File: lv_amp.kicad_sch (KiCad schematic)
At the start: 80 parts, among them J1 AudioJack2, J2 Jack-DC, J3 AudioJack2, Q1 Q_NMOS_DGS, U1 ECC83, U2 TL072, U3 ECC83, U4 ECC83, U5 MAX1771xSA

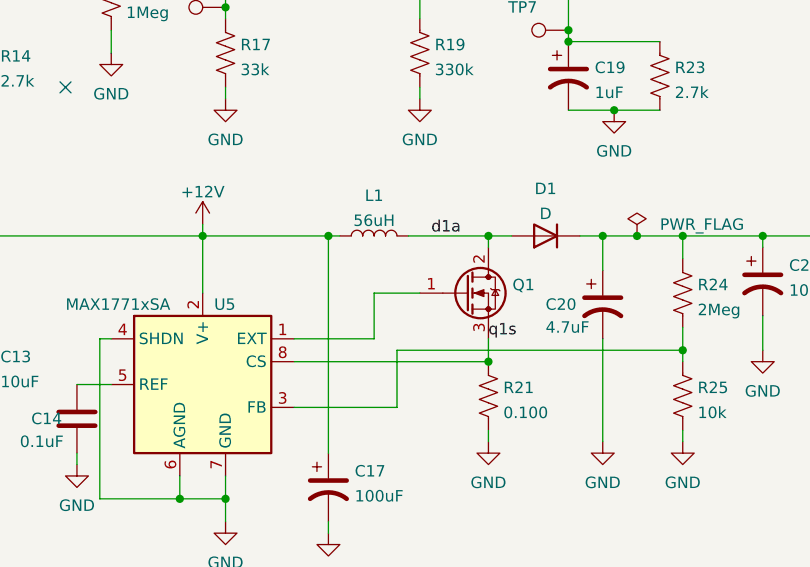
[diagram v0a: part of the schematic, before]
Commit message: power supply layout
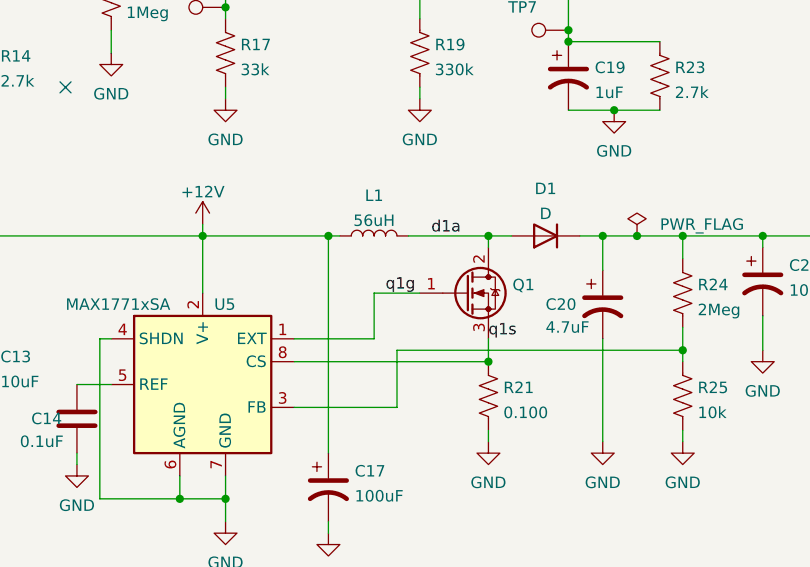
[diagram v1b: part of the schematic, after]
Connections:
- net q1g: now reaches Q1.1 (G), U5.1 (EXT)
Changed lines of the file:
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@@
+    (effects (font (size 1.27 1.27)) (justify left bottom))
+  )
+  (label "q1g" (at 170.18 125.73 0)
     (effects (font (size 1.27 1.27)) (justify left bottom))
   )

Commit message: tighter layout
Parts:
- removed TP1, TP5, TP6, TP7, TP8: TestPoint, TestPoint:TestPoint_THTPad_2.0x2.0mm_Drill1.0mm, symbol Connector:TestPoint
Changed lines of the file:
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@@
   (junction (at 85.09 157.48) (diameter 0) (color 0 0 0 0)
   )
-  (junction (at 152.4 93.98) (diameter 0) (color 0 0 0 0)
-  )
   (junction (at 48.26 143.51) (diameter 0) (color 0 0 0 0)
   )
@@
   (junction (at 193.04 69.85) (diameter 0) (color 0 0 0 0)
   )
-  (junction (at 190.5 96.52) (diameter 0) (color 0 0 0 0)
-  )
   (junction (at 194.31 119.38) (diameter 0) (color 0 0 0 0)
   )
@@
   (junction (at 29.21 152.4) (diameter 0) (color 0 0 0 0)
   )
-  (junction (at 240.03 93.98) (diameter 0) (color 0 0 0 0)
-  )
   (junction (at 267.97 76.2) (diameter 0) (color 0 0 0 0)
   )
@@
   (junction (at 64.77 160.02) (diameter 0) (color 0 0 0 0)
   )
-  (junction (at 115.57 95.25) (diameter 0) (color 0 0 0 0)
-  )
   (junction (at 59.69 72.39) (diameter 0) (color 0 0 0 0)
   )
@@
   (junction (at 154.94 189.23) (diameter 0) (color 0 0 0 0)
   )
-  (junction (at 57.15 96.52) (diameter 0) (color 0 0 0 0)
-  )
   (junction (at 73.66 72.39) (diameter 0) (color 0 0 0 0)
   )
@@
     (stroke (width 0) (type default) (color 0 0 0 0))
   )
-  (wire (pts (xy 115.57 95.25) (xy 115.57 96.52))
+  (wire (pts (xy 115.57 92.71) (xy 115.57 96.52))
     (stroke (width 0) (type default) (color 0 0 0 0))
   )
-  (wire (pts (xy 152.4 93.98) (xy 152.4 95.25))
+  (wire (pts (xy 152.4 92.71) (xy 152.4 95.25))
     (stroke (width 0) (type default) (color 0 0 0 0))
   )
@@
     (stroke (width 0) (type default) (color 0 0 0 0))
   )
-  (wire (pts (xy 190.5 92.71) (xy 190.5 96.52))
+  (wire (pts (xy 190.5 92.71) (xy 190.5 97.79))
     (stroke (width 0) (type default) (color 0 0 0 0))
   )
@@
     (stroke (width 0) (type default) (color 0 0 0 0))
   )
-  (wire (pts (xy 57.15 96.52) (xy 57.15 97.79))
+  (wire (pts (xy 57.15 93.98) (xy 57.15 97.79))
     (stroke (width 0) (type default) (color 0 0 0 0))
   )
@@
     (stroke (width 0) (type default) (color 0 0 0 0))
   )
-  (wire (pts (xy 57.15 93.98) (xy 57.15 96.52))
-    (stroke (width 0) (type default) (color 0 0 0 0))
-  )
   (wire (pts (xy 82.55 72.39) (xy 85.09 72.39))
     (stroke (width 0) (type default) (color 0 0 0 0))
@@
     (stroke (width 0) (type default) (color 0 0 0 0))
   )
-  (wire (pts (xy 115.57 92.71) (xy 115.57 95.25))
-    (stroke (width 0) (type default) (color 0 0 0 0))
-  )
   (wire (pts (xy 73.66 72.39) (xy 73.66 63.5))
     (stroke (width 0) (type default) (color 0 0 0 0))
@@
     (stroke (width 0) (type default) (color 0 0 0 0))
   )
-  (wire (pts (xy 152.4 92.71) (xy 152.4 93.98))
-    (stroke (width 0) (type default) (color 0 0 0 0))
-  )
   (wire (pts (xy 35.56 96.52) (xy 35.56 100.33))
     (stroke (width 0) (type default) (color 0 0 0 0))
@@
     (stroke (width 0) (type default) (color 0 0 0 0))
   )
-  (wire (pts (xy 240.03 90.17) (xy 240.03 93.98))
+  (wire (pts (xy 240.03 90.17) (xy 240.03 95.25))
     (stroke (width 0) (type default) (color 0 0 0 0))
   )
@@
     (stroke (width 0) (type default) (color 0 0 0 0))
   )
-  (wire (pts (xy 240.03 93.98) (xy 240.03 95.25))
-    (stroke (width 0) (type default) (color 0 0 0 0))
-  )
   (wire (pts (xy 118.11 40.64) (xy 118.11 44.45))
     (stroke (width 0) (type default) (color 0 0 0 0))
   )
-  (wire (pts (xy 190.5 96.52) (xy 190.5 97.79))
-    (stroke (width 0) (type default) (color 0 0 0 0))
-  )
   (wire (pts (xy 57.15 97.79) (xy 67.31 97.79))
     (stroke (width 0) (type default) (color 0 0 0 0))
@@
     (pin "1")
   )
-  (symbol (lib_id "Connector:TestPoint") (at 190.5 96.52 90) (unit 1)
-    (in_bom yes) (on_board yes)
-    (property "Reference" "TP7" (id 0) (at 185.42 93.98 90))
-    (property "Value" "TestPoint" (id 1) (at 187.198 94.6936 90)
-      (effects (font (size 1.27 1.27)) hide)
-    )
-    (property "Footprint" "TestPoint:TestPoint_THTPad_2.0x2.0mm_Drill1.0mm" (id 2) (at 190.5 91.44 0)
-      (effects (font (size 1.27 1.27)) hide)
-    )
-    (property "Datasheet" "~" (id 3) (at 190.5 91.44 0)
-      (effects (font (size 1.27 1.27)) hide)
-    )
-    (pin "1")
-  )
   (symbol (lib_id "power:+12V") (at 111.76 43.18 180) (unit 1)
     (in_bom yes) (on_board yes) (fields_autoplaced)
@@
     (pin "1")
   )
-  (symbol (lib_id "Connector:TestPoint") (at 152.4 93.98 90) (unit 1)
-    (in_bom yes) (on_board yes)
-    (property "Reference" "TP6" (id 0) (at 148.59 91.44 90))
-    (property "Value" "TestPoint" (id 1) (at 149.098 92.1536 90)
-      (effects (font (size 1.27 1.27)) hide)
-    )
-    (property "Footprint" "TestPoint:TestPoint_THTPad_2.0x2.0mm_Drill1.0mm" (id 2) (at 152.4 88.9 0)
-      (effects (font (size 1.27 1.27)) hide)
-    )
-    (property "Datasheet" "~" (id 3) (at 152.4 88.9 0)
-      (effects (font (size 1.27 1.27)) hide)
-    )
-    (pin "1")
-  )
   (symbol (lib_id "power:PWR_FLAG") (at 109.22 119.38 180) (unit 1)
     (in_bom yes) (on_board yes) (fields_autoplaced)
@@
     (pin "2")
   )
-  (symbol (lib_id "Connector:TestPoint") (at 240.03 93.98 90) (unit 1)
-    (in_bom yes) (on_board yes)
-    (property "Reference" "TP8" (id 0) (at 234.95 91.44 90))
-    (property "Value" "TestPoint" (id 1) (at 236.728 92.1536 90)
-      (effects (font (size 1.27 1.27)) hide)
-    )
-    (property "Footprint" "TestPoint:TestPoint_THTPad_2.0x2.0mm_Drill1.0mm" (id 2) (at 240.03 88.9 0)
-      (effects (font (size 1.27 1.27)) hide)
-    )
-    (property "Datasheet" "~" (id 3) (at 240.03 88.9 0)
-      (effects (font (size 1.27 1.27)) hide)
-    )
-    (pin "1")
-  )
   (symbol (lib_id "power:HT") (at 118.11 44.45 180) (unit 1)
     (in_bom yes) (on_board yes) (fields_autoplaced)
@@
     (pin "1")
   )
-  (symbol (lib_id "Connector:TestPoint") (at 57.15 96.52 90) (unit 1)
-    (in_bom yes) (on_board yes)
-    (property "Reference" "TP1" (id 0) (at 52.07 93.98 90))
-    (property "Value" "TestPoint" (id 1) (at 53.848 94.6936 90)
-      (effects (font (size 1.27 1.27)) hide)
-    )
-    (property "Footprint" "TestPoint:TestPoint_THTPad_2.0x2.0mm_Drill1.0mm" (id 2) (at 57.15 91.44 0)
-      (effects (font (size 1.27 1.27)) hide)
-    )
-    (property "Datasheet" "~" (id 3) (at 57.15 91.44 0)
-      (effects (font (size 1.27 1.27)) hide)
-    )
-    (pin "1")
-  )
   (symbol (lib_id "Device:C_Polarized_US") (at 124.46 134.62 0) (unit 1)
     (in_bom yes) (on_board yes) (fields_autoplaced)
@@
     (pin "1")
   )
-  (symbol (lib_id "Connector:TestPoint") (at 115.57 95.25 90) (unit 1)
-    (in_bom yes) (on_board yes)
-    (property "Reference" "TP5" (id 0) (at 110.49 92.71 90))
-    (property "Value" "TestPoint" (id 1) (at 112.268 93.4236 90)
-      (effects (font (size 1.27 1.27)) hide)
-    )
-    (property "Footprint" "TestPoint:TestPoint_THTPad_2.0x2.0mm_Drill1.0mm" (id 2) (at 115.57 90.17 0)
-      (effects (font (size 1.27 1.27)) hide)
-    )
-    (property "Datasheet" "~" (id 3) (at 115.57 90.17 0)
-      (effects (font (size 1.27 1.27)) hide)
-    )
-    (pin "1")
-  )
   (symbol (lib_id "Valve:ECC83") (at 73.66 29.21 0) (unit 3)
     (in_bom yes) (on_board yes) (fields_autoplaced)
@@
       (reference "RV4") (unit 1) (value "500k") (footprint "Potentiometer_THT:Potentiometer_Piher_T-16H_Single_Horizontal")
     )
-    (path "/72b96fdc-17eb-4ecb-ae5d-68b51cd75350"
-      (reference "TP1") (unit 1) (value "TestPoint") (footprint "TestPoint:TestPoint_THTPad_2.0x2.0mm_Drill1.0mm")
-    )
     (path "/6e1639bd-21ca-4f2f-b6f4-6dbea494eb53"
       (reference "TP2") (unit 1) (value "TestPoint") (footprint "TestPoint:TestPoint_THTPad_2.0x2.0mm_Drill1.0mm")
@@
       (reference "TP4") (unit 1) (value "TestPoint") (footprint "TestPoint:TestPoint_THTPad_2.0x2.0mm_Drill1.0mm")
     )
-    (path "/beffb8e8-cbb0-4bb3-bc79-ad300693e67c"
-      (reference "TP5") (unit 1) (value "TestPoint") (footprint "TestPoint:TestPoint_THTPad_2.0x2.0mm_Drill1.0mm")
-    )
-    (path "/1d857cb6-ac9c-45f8-a53f-50be7ba59418"
-      (reference "TP6") (unit 1) (value "TestPoint") (footprint "TestPoint:TestPoint_THTPad_2.0x2.0mm_Drill1.0mm")
-    )
-    (path "/0fc25247-064e-4a99-a2d0-b21a85dfd649"
-      (reference "TP7") (unit 1) (value "TestPoint") (footprint "TestPoint:TestPoint_THTPad_2.0x2.0mm_Drill1.0mm")
-    )
-    (path "/5d591f3c-2404-4803-a07e-13d37c52af18"
-      (reference "TP8") (unit 1) (value "TestPoint") (footprint "TestPoint:TestPoint_THTPad_2.0x2.0mm_Drill1.0mm")
-    )
     (path "/24fe7676-0c0a-4b5a-8a61-dd833b2a3e83"

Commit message: route/re-annotate
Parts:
- added H1, H2, H3, H4: MountingHole_Pad, MountingHole:MountingHole_3.2mm_M3, symbol Mechanical:MountingHole_Pad
- renumbered C22 to C1, C5 to C11, C7 to C12, C3 to C13, C2 to C14, C8 to C15, C23 to C16, C12 to C17, C9 to C18, C16 to C19, C1 to C2, C21 to C20, C18 to C21, C4 to C22, C6 to C23, C19 to C3, C13 to C4, C20 to C5, C11 to C6, C14 to C7, C17 to C8, C15 to C9, J2 to J1, J3 to J2, J1 to J3, R32 to R1, R21 to R10, R28 to R11, R27 to R12, R26 to R13, R15 to R14, R18 to R15, R12 to R17, R22 to R18, R7 to R19, R31 to R2, R14 to R20, R5 to R21, R4 to R22, R13 to R23, R8 to R24, R3 to R25, R2 to R26, R9 to R27, R17 to R28, R20 to R29, R30 to R3, R6 to R30, R19 to R31, R10 to R32, R11 to R33, R29 to R4, R25 to R5, R24 to R6, R1 to R7, R33 to R8, R23 to R9, RV4 to RV1, RV1 to RV3, RV3 to RV4, TP4 to TP1, TP9 to TP4, U5 to U1, U4 to U3, U3 to U4, U1 to U5
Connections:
- net GND: now also H1.1, H2.1, H3.1, H4.1

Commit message: tweaks
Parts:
- renumbered C23 to C21, C21 to C22, C22 to C23, R11 to R10, R10 to R11, R17 to R15, R18 to R16, R15 to R17, R16 to R18, R20 to R19, R19 to R20, R23 to R22, R24 to R23, R22 to R24, R27 to R26, R29 to R27, R26 to R29, R7 to R4, R8 to R5, R4 to R6, R5 to R7, R6 to R8

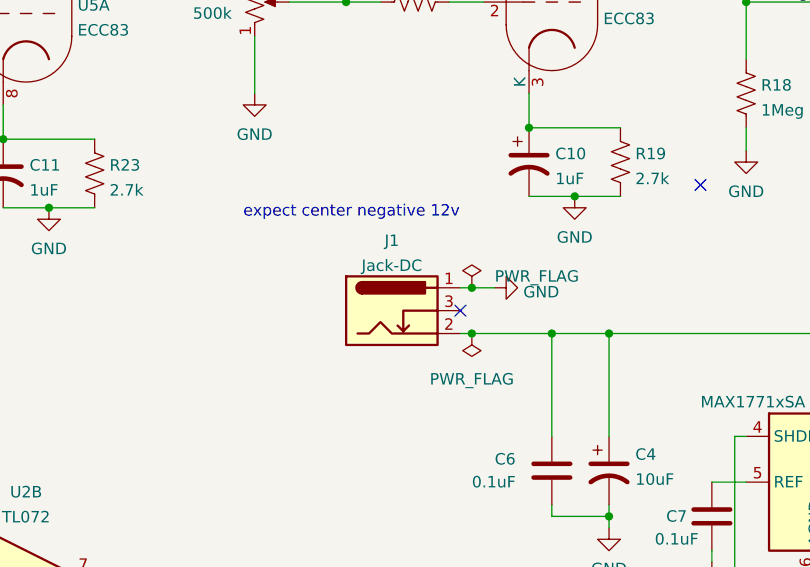
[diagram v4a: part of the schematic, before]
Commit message: alpha0 errata: DC jack
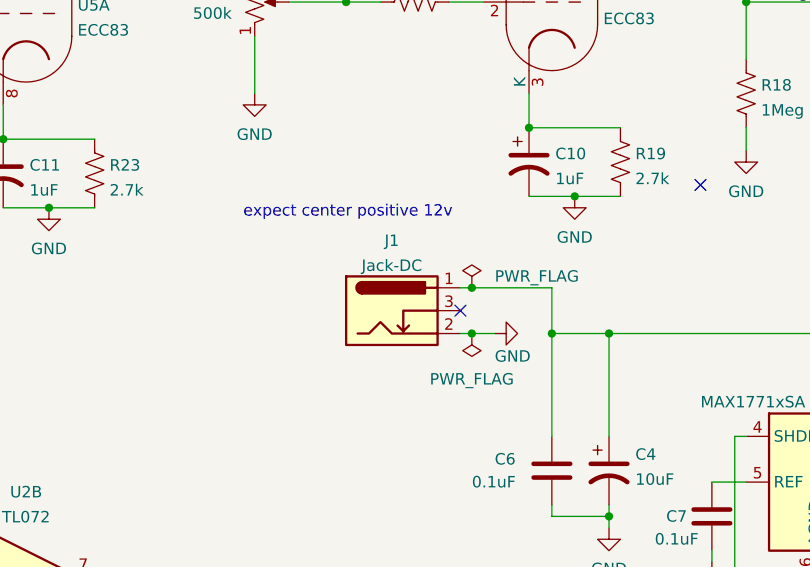
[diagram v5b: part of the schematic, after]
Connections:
- net +12V: now also J1.1; no longer J1.2
- net GND: now also J1.2; no longer J1.1
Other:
- note added: "expect center positive 12v"
- note removed: "expect center negative 12v"
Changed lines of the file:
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@@
   (junction (at 95.25 82.55) (diameter 0) (color 0 0 0 0)
   )
+  (junction (at 254 76.2) (diameter 0) (color 0 0 0 0)
+  )
+  (junction (at 29.21 168.91) (diameter 0) (color 0 0 0 0)
+  )
+  (junction (at 163.83 119.38) (diameter 0) (color 0 0 0 0)
+  )
+  (junction (at 203.2 132.08) (diameter 0) (color 0 0 0 0)
+  )
+  (junction (at 173.99 82.55) (diameter 0) (color 0 0 0 0)
+  )
+  (junction (at 85.09 157.48) (diameter 0) (color 0 0 0 0)
+  )
+  (junction (at 48.26 143.51) (diameter 0) (color 0 0 0 0)
+  )
+  (junction (at 222.25 80.01) (diameter 0) (color 0 0 0 0)
+  )
+  (junction (at 67.31 152.4) (diameter 0) (color 0 0 0 0)
+  )
+  (junction (at 190.5 97.79) (diameter 0) (color 0 0 0 0)
+  )
+  (junction (at 57.15 97.79) (diameter 0) (color 0 0 0 0)
+  )
+  (junction (at 35.56 83.82) (diameter 0) (color 0 0 0 0)
+  )
+  (junction (at 118.11 69.85) (diameter 0) (color 0 0 0 0)
+  )
+  (junction (at 26.67 81.28) (diameter 0) (color 0 0 0 0)
+  )
+  (junction (at 181.61 119.38) (diameter 0) (color 0 0 0 0)
+  )
+  (junction (at 181.61 133.35) (diameter 0) (color 0 0 0 0)
+  )
+  (junction (at 109.22 114.3) (diameter 0) (color 0 0 0 0)
+  )
+  (junction (at 193.04 69.85) (diameter 0) (color 0 0 0 0)
+  )
   (junction (at 118.11 119.38) (diameter 0) (color 0 0 0 0)
   )
-  (junction (at 254 76.2) (diameter 0) (color 0 0 0 0)
-  )
   (junction (at 109.22 119.38) (diameter 0) (color 0 0 0 0)
-  )
-  (junction (at 29.21 168.91) (diameter 0) (color 0 0 0 0)
-  )
-  (junction (at 163.83 119.38) (diameter 0) (color 0 0 0 0)
-  )
-  (junction (at 203.2 132.08) (diameter 0) (color 0 0 0 0)
-  )
-  (junction (at 173.99 82.55) (diameter 0) (color 0 0 0 0)
-  )
-  (junction (at 85.09 157.48) (diameter 0) (color 0 0 0 0)
-  )
-  (junction (at 48.26 143.51) (diameter 0) (color 0 0 0 0)
-  )
-  (junction (at 222.25 80.01) (diameter 0) (color 0 0 0 0)
-  )
-  (junction (at 67.31 152.4) (diameter 0) (color 0 0 0 0)
-  )
-  (junction (at 190.5 97.79) (diameter 0) (color 0 0 0 0)
-  )
-  (junction (at 57.15 97.79) (diameter 0) (color 0 0 0 0)
-  )
-  (junction (at 35.56 83.82) (diameter 0) (color 0 0 0 0)
-  )
-  (junction (at 118.11 69.85) (diameter 0) (color 0 0 0 0)
-  )
-  (junction (at 26.67 81.28) (diameter 0) (color 0 0 0 0)
-  )
-  (junction (at 181.61 119.38) (diameter 0) (color 0 0 0 0)
-  )
-  (junction (at 181.61 133.35) (diameter 0) (color 0 0 0 0)
-  )
-  (junction (at 109.22 114.3) (diameter 0) (color 0 0 0 0)
-  )
-  (junction (at 193.04 69.85) (diameter 0) (color 0 0 0 0)
   )
   (junction (at 194.31 119.38) (diameter 0) (color 0 0 0 0)
@@
     (stroke (width 0) (type default) (color 0 0 0 0))
   )
+  (wire (pts (xy 118.11 114.3) (xy 118.11 119.38))
+    (stroke (width 0) (type default) (color 0 0 0 0))
+  )
   (wire (pts (xy 254 74.93) (xy 254 76.2))
     (stroke (width 0) (type default) (color 0 0 0 0))
@@
     (stroke (width 0) (type default) (color 0 0 0 0))
   )
-  (wire (pts (xy 109.22 114.3) (xy 111.76 114.3))
+  (wire (pts (xy 109.22 114.3) (xy 118.11 114.3))
     (stroke (width 0) (type default) (color 0 0 0 0))
   )
@@
     (stroke (width 0) (type default) (color 0 0 0 0))
   )
+  (wire (pts (xy 109.22 119.38) (xy 111.76 119.38))
+    (stroke (width 0) (type default) (color 0 0 0 0))
+  )
   (wire (pts (xy 139.7 130.81) (xy 138.43 130.81))
     (stroke (width 0) (type default) (color 0 0 0 0))
@@
   )
   (wire (pts (xy 195.58 105.41) (xy 200.66 105.41))
-    (stroke (width 0) (type default) (color 0 0 0 0))
-  )
-  (wire (pts (xy 109.22 119.38) (xy 118.11 119.38))
     (stroke (width 0) (type default) (color 0 0 0 0))
   )
@@
     (effects (font (size 1.27 1.27)) (justify left bottom))
   )
-  (text "expect center negative 12v" (at 83.82 106.68 0)
+  (text "expect center positive 12v" (at 83.82 106.68 0)
     (effects (font (size 1.27 1.27)) (justify left bottom))
   )
@@
     (pin "2")
   )
-  (symbol (lib_id "power:GND") (at 111.76 114.3 90) (unit 1)
-    (in_bom yes) (on_board yes) (fields_autoplaced)
-    (property "Reference" "#PWR018" (id 0) (at 118.11 114.3 0)
-      (effects (font (size 1.27 1.27)) hide)
-    )
-    (property "Value" "GND" (id 1) (at 114.935 114.779 90)
+  (symbol (lib_id "power:GND") (at 111.76 119.38 90) (unit 1)
+    (in_bom yes) (on_board yes)
+    (property "Reference" "#PWR018" (id 0) (at 118.11 119.38 0)
+      (effects (font (size 1.27 1.27)) hide)
+    )
+    (property "Value" "GND" (id 1) (at 111.76 121.92 90)
       (effects (font (size 1.27 1.27)) (justify right))
     )
-    (property "Footprint" "" (id 2) (at 111.76 114.3 0)
-      (effects (font (size 1.27 1.27)) hide)
-    )
-    (property "Datasheet" "" (id 3) (at 111.76 114.3 0)
-      (effects (font (size 1.27 1.27)) hide)
-    )
+    (property "Footprint" "" (id 2) (at 111.76 119.38 0)
+      (effects (font (size 1.27 1.27)) hide)
+    )
+    (property "Datasheet" "" (id 3) (at 111.76 119.38 0)
+      (effects (font (size 1.27 1.27)) hide)
+    )
